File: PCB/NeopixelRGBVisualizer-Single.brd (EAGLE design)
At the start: 55 x 30 mm, 23 parts, among them CN2 5-12VDC, IC1 MSGEQ7, IC2 78L05ACZ-AP, Q1 16MHz, X1 STEREOJACK

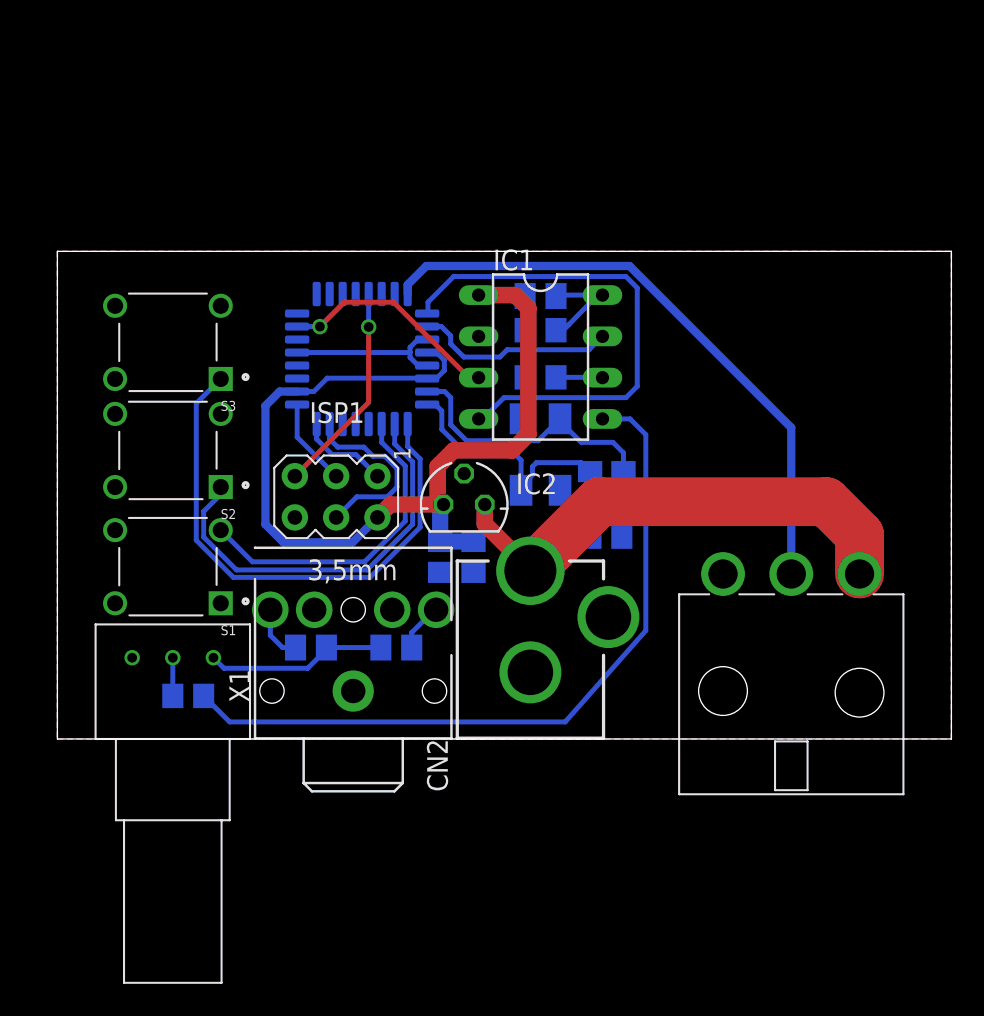
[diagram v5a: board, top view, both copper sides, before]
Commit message: Prototype version 2 with buttons and Molex minifit jr connector with shape appropriate for project boxes
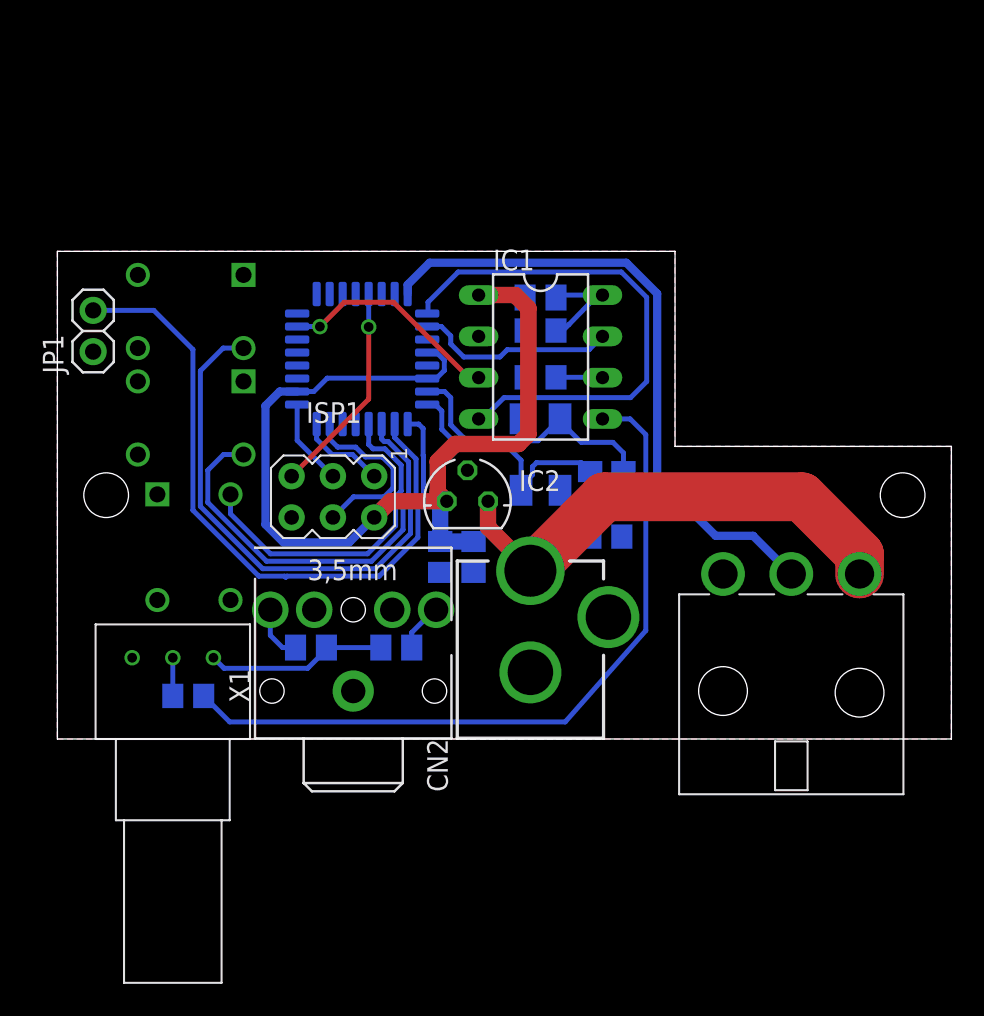
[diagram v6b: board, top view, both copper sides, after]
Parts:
- added JP1: POWER BUTTON, mypinhead:1X02-ROUND
- S1, S2, S3: value 2-1825910-7 -> 2-1825910-5; device 2-1825910-7:SW_2-1825910-7 -> te_tactileswitch:SW_2-1825910
- moved S2 2.44 mm to (8.20, 19.8), flipped to the bottom, turned to 0 degrees
- moved S3 2.36 mm to (8.20, 26.3), flipped to the bottom, turned to 0 degrees
- moved S1 2.00 mm to (8.40, 11.8), flipped to the bottom, turned to 270 degrees
- moved IC2 0.28 mm to (25.2, 14.6)
- moved ISP1 0.20 mm to (16.9, 14.9)
- moved R3 0.09 mm to (29.7, 27.2)
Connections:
- net N$7 renamed MSGEQ7_OUT
- net N$8 renamed MSGEQ7_STROBE
- net N$9 renamed MSGEQ7_RESET
- new net N$8: S2.2, U$1.11
- net GND: now also JP1.1
- net N$18: now also U$1.12; no longer U$1.11
- net N$19: now also S3.2; no longer S2.1
- net N$20: now also JP1.2; no longer S3.1
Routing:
- net N$8: track 0.00 -> 26.4 mm
- net GND: track 10.1 -> 0.57 mm
- net N$19: track 25.0 -> 34.4 mm
- net N$20: track 33.2 -> 41.5 mm
- net N$17: track 37.8 -> 39.3 mm
- net N$18: track 19.8 -> 20.7 mm
- net MSGEQ7_STROBE: track 31.2 -> 32.1 mm
- net VCC: track 60.8 -> 61.5 mm
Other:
- outline, holes or cut-outs redrawn

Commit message: Partially completed silkscreen for v2 production
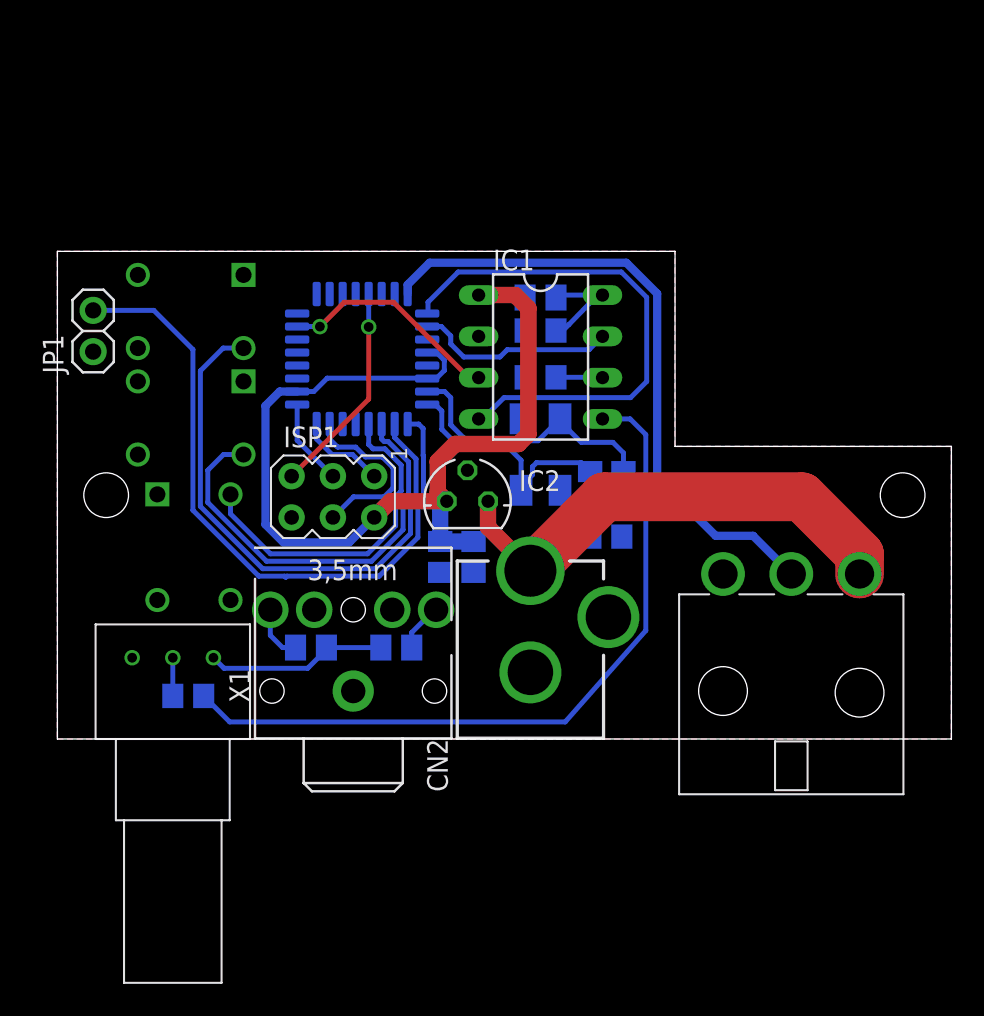
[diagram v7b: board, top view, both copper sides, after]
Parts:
- JP1: value POWER BUTTON -> 1/0
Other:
- board text added: "EricMakesEverything"
- board text added: "NeoPixel Visualizer"
- board text added: "v2"

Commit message: Resized board to try to sqeeze it into the project box easier, made a cutout section for a big friendly panel-mount power button, and moved descriptive text from the tdocu layer to the tnames layer to be compatible with the CAM file supplied by Oshpark.
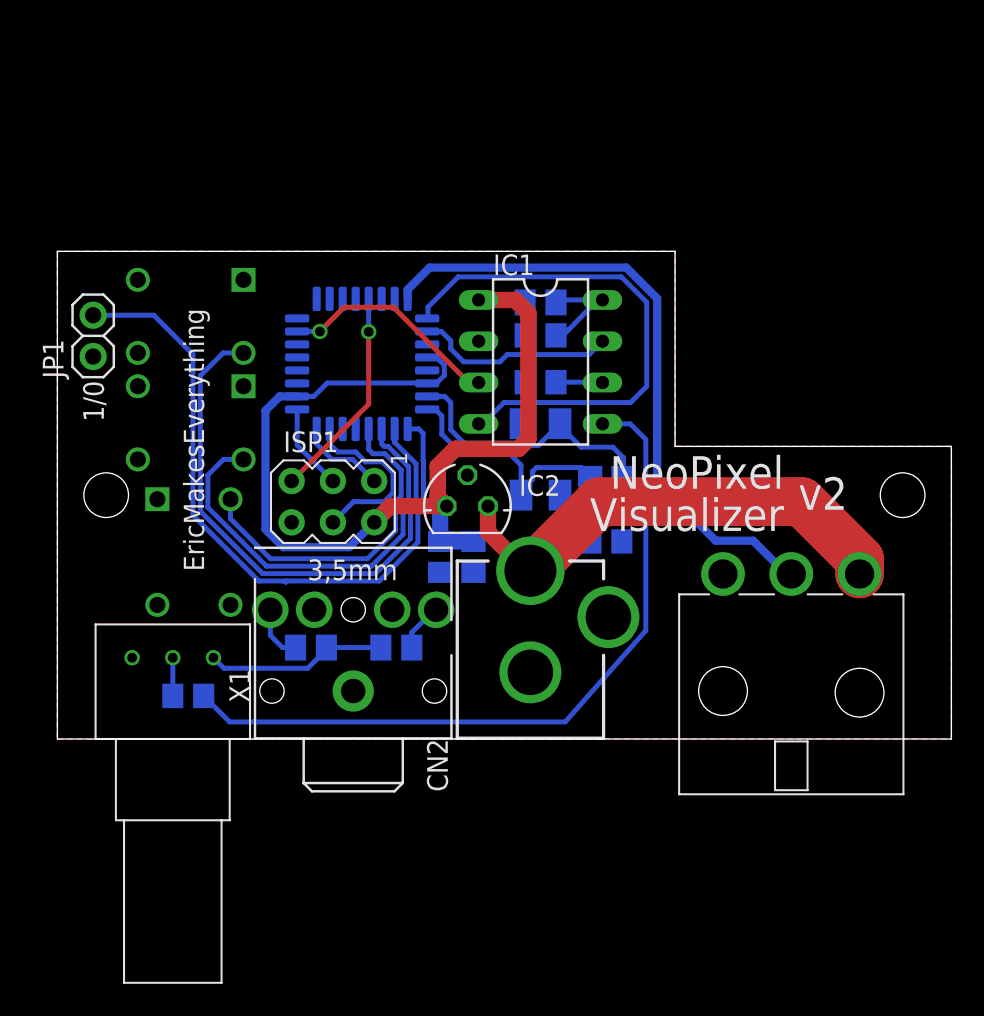
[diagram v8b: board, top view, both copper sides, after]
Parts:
- moved C2 0.30 mm to (29.7, 24.8)
- moved C4 0.30 mm to (29.7, 21.9)
- moved C5 0.30 mm to (34.8, 15.2)
- moved C6 0.30 mm to (32.8, 15.2)
- moved IC1 0.30 mm to (29.7, 23.2)
- moved IC2 0.30 mm to (25.2, 14.3)
- moved ISP1 0.30 mm to (16.9, 14.6)
- moved JP1 0.30 mm to (2.20, 24.8)
- moved Q1 0.30 mm to (29.7, 17.2)
- moved R3 0.30 mm to (29.7, 26.9)
- moved S1 0.30 mm to (8.40, 11.5)
- moved S2 0.30 mm to (8.20, 19.4)
- moved S3 0.30 mm to (8.20, 26.0)
- moved U$1 0.30 mm to (18.8, 23.1)
- moved C8 0.30 mm to (33.8, 12.2)
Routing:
- net VIN: track 34.8 -> 34.0 mm
- net GND: track 0.57 -> 0.00 mm
